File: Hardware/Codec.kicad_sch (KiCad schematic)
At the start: 17 parts, among them U5 CS4272

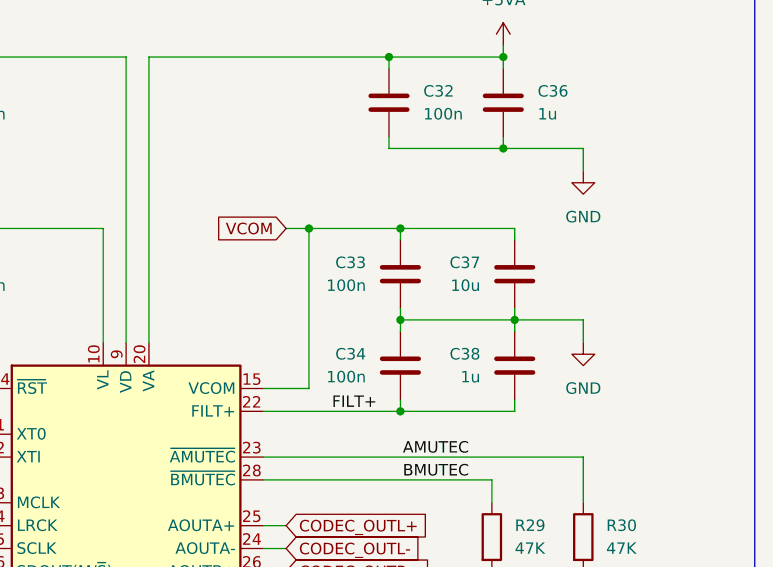
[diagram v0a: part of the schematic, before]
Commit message: Silkscreen and notes
Updated the board silkscreen.
Updated VCOM capacitance value.
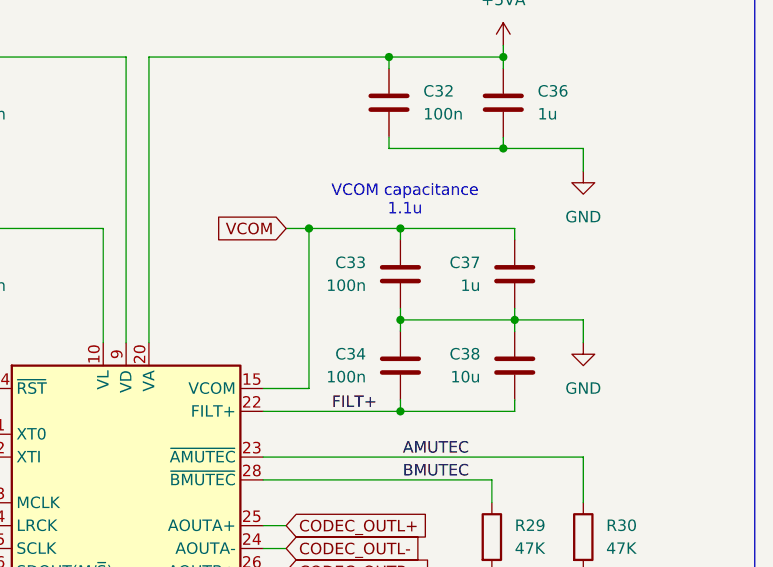
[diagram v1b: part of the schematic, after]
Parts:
- C37: value 10u -> 1u
- C38: value 1u -> 10u
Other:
- note added: "VCOM capacitance 1.1u"
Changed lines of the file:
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@@
 		(company "DavidMolTor")
 	)
+	(text "VCOM capacitance\n1.1u"
+		(exclude_from_sim no)
+		(at 168.148 66.802 0)
+		(effects
+			(font
+				(size 1.27 1.27)
+			)
+		)
+	)
 	(text_box "AUDIO CODEC"
 		(exclude_from_sim no)
@@
 			)
 		)
-		(property "Value" "1u"
+		(property "Value" "10u"
 			(at 176.53 86.3601 0)
 			(show_name no)
@@
 			)
 		)
-		(property "Value" "10u"
+		(property "Value" "1u"
 			(at 176.53 76.1999 0)
 			(show_name no)
